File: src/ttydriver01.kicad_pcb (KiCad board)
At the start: 2 copper layers, 119.4 x 62.2 mm, 29 parts, among them P1 CONN_01X04, P2 CONN_01X02, P3 CONN_01X02, Q1 IRLB8721PBF, T1 Coilcraft-DA2032, U1 NE555, U2 TPS2030P, U3 CP2102-breakout, U4 G3VM401E

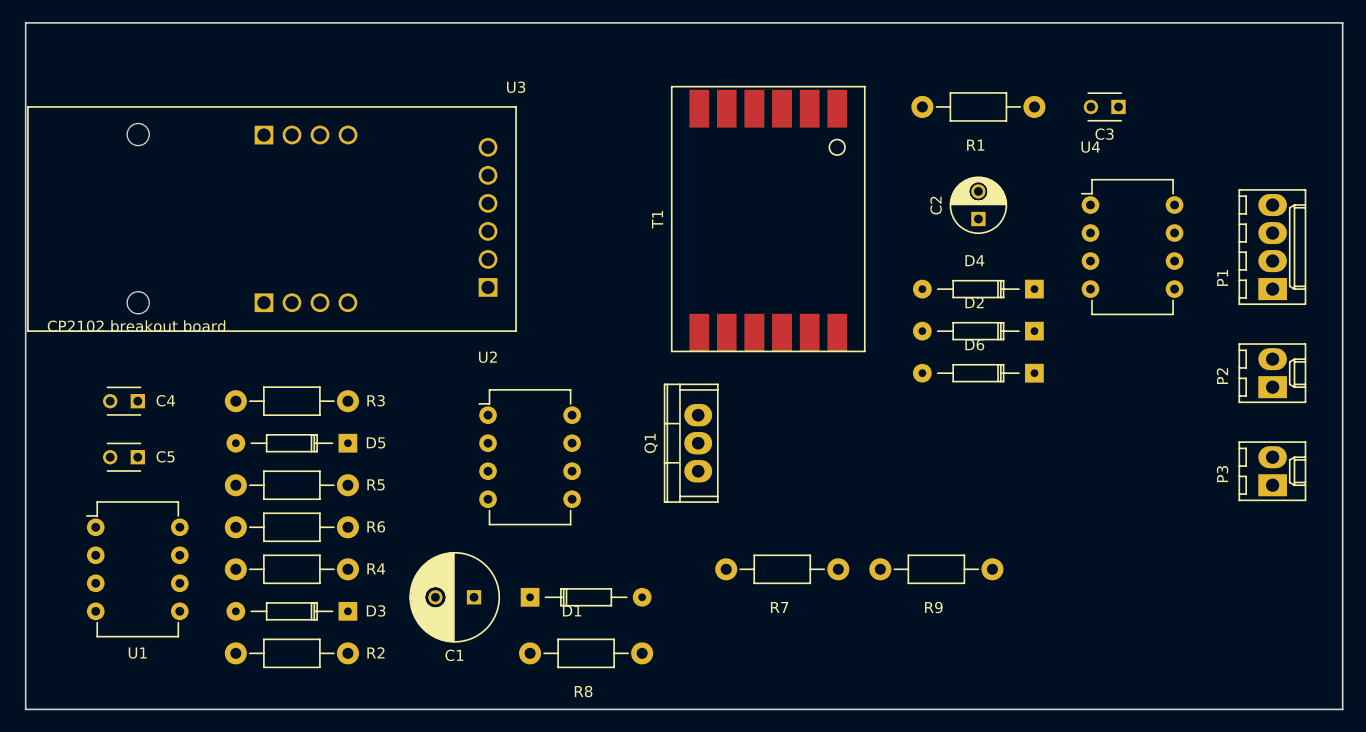
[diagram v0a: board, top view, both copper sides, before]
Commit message: Add 24VDC supply for keyboard
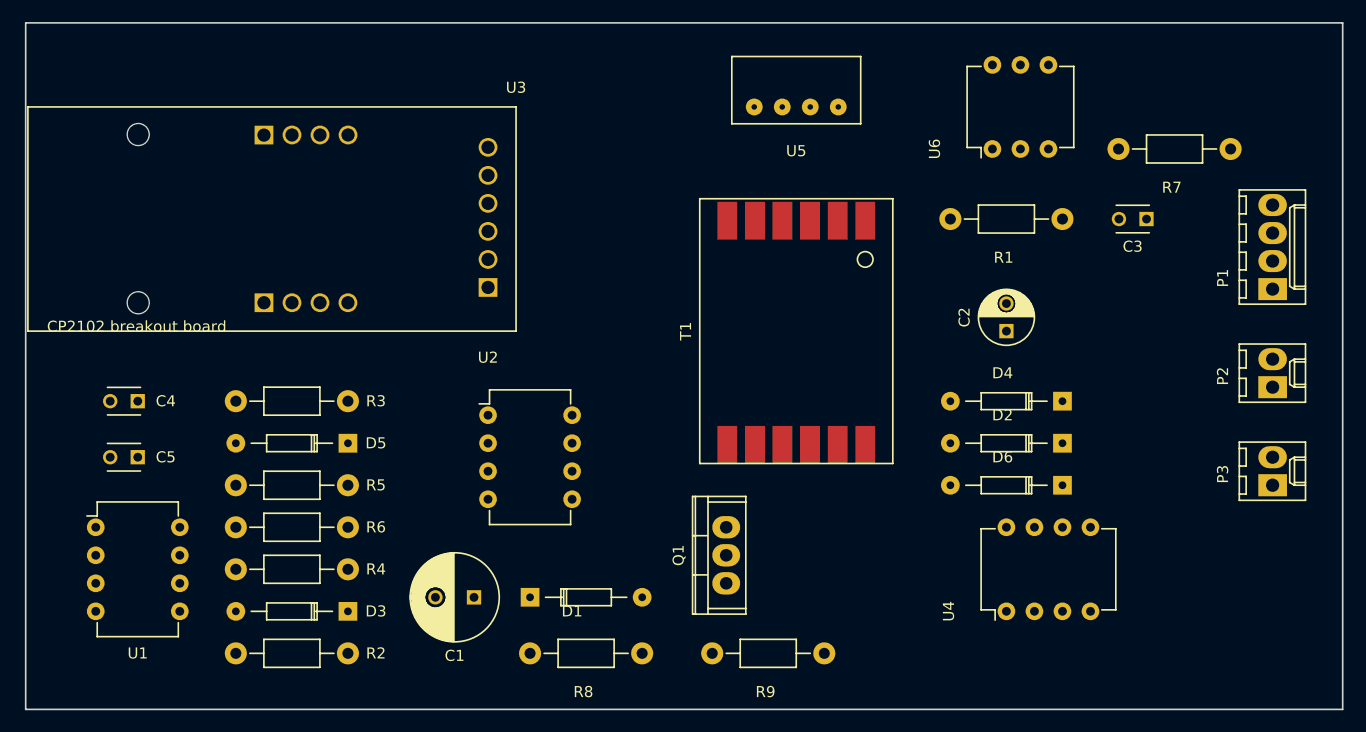
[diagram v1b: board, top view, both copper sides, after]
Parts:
- added U5: IE0524S, DC-DC:IE0524S, F.Cu at (125.7, 97.8)
- added U6: G3VM401E, Housings_DIP:DIP-6_W7.62mm, F.Cu at (143.5, 101.6)
- R7: value 1K -> 3.3K
- R9: value 1K -> 680
- moved R7 52.1 mm to (165.1, 101.6)
- moved U4 37.6 mm to (144.8, 143.5), turned to 90 degrees
- moved R9 17.0 mm to (128.3, 147.3)
- moved D2 10.5 mm to (149.9, 128.3)
- moved D6 10.5 mm to (149.9, 132.1)
- moved D4 10.5 mm to (149.9, 124.5)
- moved R1 10.5 mm to (149.9, 108.0)
- moved T1 10.5 mm to (125.7, 118.1)
- moved C2 10.5 mm to (144.8, 118.1)
- moved C3 10.5 mm to (157.5, 108.0)
- moved Q1 10.5 mm to (119.4, 138.4)
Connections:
- net /TXd renamed /TxD
- U3 pad 3-4: Net-(R7-Pad2) -> /RxD

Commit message: Added footprint for DC-DC converter
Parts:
- removed R8: 1K, Resistors_ThroughHole:Resistor_Horizontal_RM10mm
- U4: footprint Housings_DIP:DIP-8_W7.62mm -> Housings_DIP:DIP-6_W7.62mm
